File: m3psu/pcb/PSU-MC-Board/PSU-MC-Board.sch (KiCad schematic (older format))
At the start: 53 parts

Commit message: Remove JTAG programmer connection from MCU board
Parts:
- removed P?: SWD_TC, agg:TC2030-NL, symbol SWD_TC
- added R? (x2): R, symbol R
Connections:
- net labels removed: ~RST
- wire segments 307 -> 385

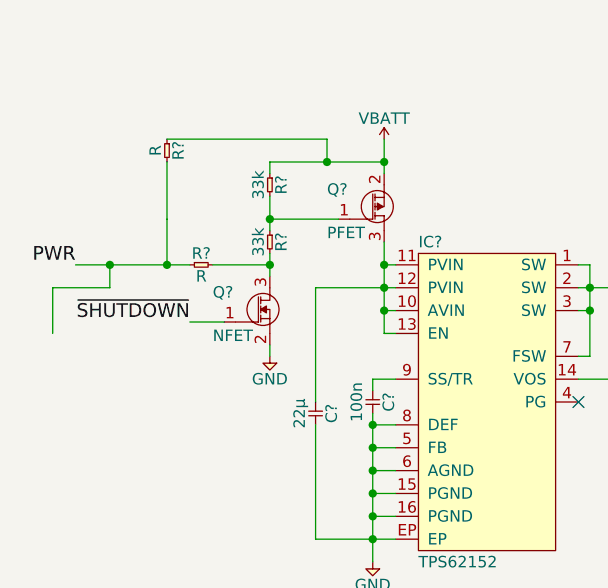
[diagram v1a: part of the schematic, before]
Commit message: Minor changes for uniformity for DC/DC converters.
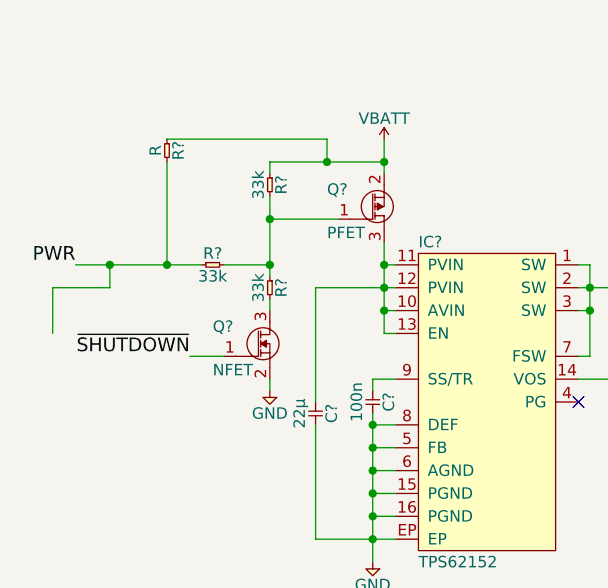
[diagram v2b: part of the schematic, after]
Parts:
- removed R?: 33k, agg:0402, symbol R
- removed R?: R, symbol R
- added R? (x2): 33k, agg:0402, symbol R
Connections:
- net PWR: now also R?.1
- net at Q?.1 (G), R?.2: now also R?.1, R?.2
- net at Q?.3 (D): now also R?.2
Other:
- moved on the sheet: Q?
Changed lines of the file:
@@
 EESchema Schematic File Version 2
 LIBS:agg-kicad
+LIBS:PSU-MC-Board-cache
 EELAYER 25 0
 EELAYER END
@@
 L NFET Q?
 U 1 1 56E1C0D3
-P 1600 1800
-F 0 "Q?" H 1350 1830 50  0000 L CNN
-F 1 "NFET" H 1350 1640 50  0000 L CNN
-F 2 "agg:SOT-883-B" H 1600 1800 50  0001 C CNN
-F 3 "http://www.nxp.com/documents/data_sheet/PMZB150UNE.pdf" H 1600 1800 50  0001 C CNN
-F 4 "2498598" H 1600 1800 60  0001 C CNN "Farnell"
-	1    1600 1800
+P 1600 1950
+F 0 "Q?" H 1350 1980 50  0000 L CNN
+F 1 "NFET" H 1350 1790 50  0000 L CNN
+F 2 "agg:SOT-883-B" H 1600 1950 50  0001 C CNN
+F 3 "http://www.nxp.com/documents/data_sheet/PMZB150UNE.pdf" H 1600 1950 50  0001 C CNN
+F 4 "2498598" H 1600 1950 60  0001 C CNN "Farnell"
+	1    1600 1950
 	1    0    0    -1
 $EndComp
@@
 $EndComp
 $Comp
-L R R?
-U 1 1 56E3210E
-P 1600 1500
-F 0 "R?" H 1650 1550 50  0000 C CNN
-F 1 "33k" H 1650 1450 50  0000 C CNN
-F 2 "agg:0402" H 1600 1500 50  0001 C CNN
-F 3 "" H 1600 1500 50  0001 C CNN
-F 4 "2447160" H 1600 1500 60  0001 C CNN "Farnell"
-	1    1600 1500
-	0    1    1    0
-$EndComp
-$Comp
 L GND #PWR020
 U 1 1 56E3524C
-P 1600 2050
-F 0 "#PWR020" H 1470 2090 50  0001 L CNN
-F 1 "GND" H 1600 1950 50  0000 C CNN
-F 2 "" H 1600 2050 60  0000 C CNN
-F 3 "" H 1600 2050 60  0000 C CNN
-	1    1600 2050
+P 1600 2200
+F 0 "#PWR020" H 1470 2240 50  0001 L CNN
+F 1 "GND" H 1600 2100 50  0000 C CNN
+F 2 "" H 1600 2200 60  0000 C CNN
+F 3 "" H 1600 2200 60  0000 C CNN
+	1    1600 2200
 	-1   0    0    -1
 $EndComp
 Text Label 750  1650 2    60   ~ 0
 PWR
-Text Label 1250 1900 2    60   ~ 0
+Text Label 1250 2050 2    60   ~ 0
 ~SHUTDOWN
 $Comp
@@
 	2100 1200 2100 1250
 Wire Wire Line
-	2100 1200 1850 1200
-Wire Wire Line
-	1850 1200 1600 1200
+	1600 1200 1850 1200
+Wire Wire Line
+	1850 1200 2100 1200
 Wire Wire Line
 	1600 1200 1600 1250
@@
 	1600 1350 1600 1450
 Wire Wire Line
-	1600 1450 1600 1500
-Wire Wire Line
-	1600 1600 1600 1650
+	1600 1450 1600 1650
 Wire Wire Line
 	1600 1650 1600 1700
@@
 Connection ~ 1600 1450
 Wire Wire Line
-	1600 2000 1600 2050
+	1600 2150 1600 2200
 Connection ~ 1600 1650
 Wire Wire Line
-	1400 1900 1250 1900
+	1400 2050 1250 2050
 Wire Wire Line
 	8800 700  8800 750
@@
 Connection ~ 9050 4250
 Wire Wire Line
-	1150 1200 1150 1450
-$Comp
-L R R?
-U 1 1 56E3DB52
-P 1250 1650
-F 0 "R?" H 1300 1700 50  0000 C CNN
-F 1 "R" H 1300 1600 50  0000 C CNN
-F 2 "" H 1250 1650 50  0001 C CNN
-F 3 "" H 1250 1650 50  0001 C CNN
-	1    1250 1650
-	1    0    0    -1
-$EndComp
-Wire Wire Line
-	1350 1650 1600 1650
-Wire Wire Line
-	1250 1650 1150 1650
-Wire Wire Line
-	1150 1650 900  1650
-Wire Wire Line
-	900  1650 750  1650
+	1150 1200 1150 1650
+Wire Wire Line
+	1400 1650 1600 1650
+Wire Wire Line
+	750  1650 900  1650
+Wire Wire Line
+	900  1650 1150 1650
+Wire Wire Line
+	1150 1650 1300 1650
 Wire Wire Line
 	900  1650 900  1750
@@
 	1850 1100 1850 1200
 Connection ~ 1850 1200
-Wire Wire Line
-	1150 1450 1150 1450
-Wire Wire Line
-	1150 1450 1150 1650
 Connection ~ 1150 1650
+Wire Wire Line
+	1600 1800 1600 1850
+$Comp
+L R R?
+U 1 1 56E2D4E9
+P 1600 1700
+F 0 "R?" H 1650 1750 50  0000 C CNN
+F 1 "33k" H 1650 1650 50  0000 C CNN
+F 2 "agg:0402" H 1600 1700 50  0001 C CNN
+F 3 "" H 1600 1700 50  0001 C CNN
+F 4 "2447160" H 1600 1700 60  0001 C CNN "Farnell"
+	1    1600 1700
+	0    1    1    0
+$EndComp
+$Comp
+L R R?
+U 1 1 56E2D5A8
+P 1300 1650
+F 0 "R?" H 1350 1700 50  0000 C CNN
+F 1 "33k" H 1350 1600 50  0000 C CNN
+F 2 "agg:0402" H 1300 1650 50  0001 C CNN
+F 3 "" H 1300 1650 50  0001 C CNN
+F 4 "2447160" H 1300 1650 60  0001 C CNN "Farnell"
+	1    1300 1650
+	1    0    0    -1
+$EndComp
 $EndSCHEMATC

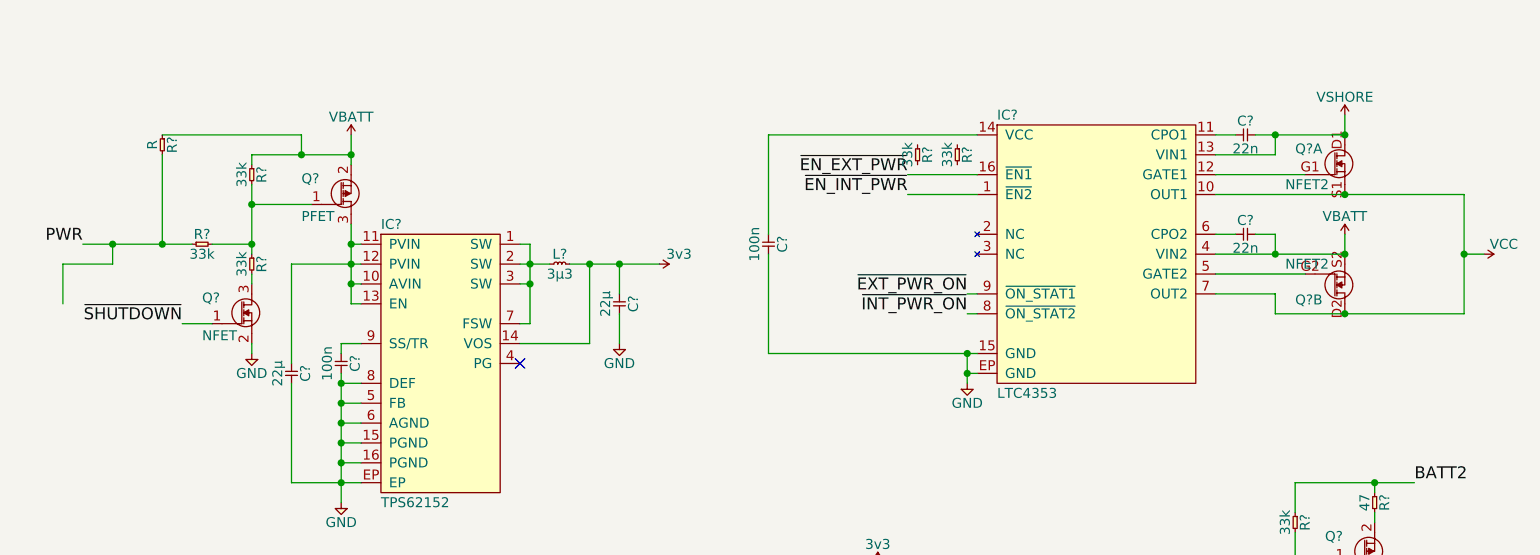
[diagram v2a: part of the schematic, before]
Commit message: Trying to resolve complete shutdown problem.
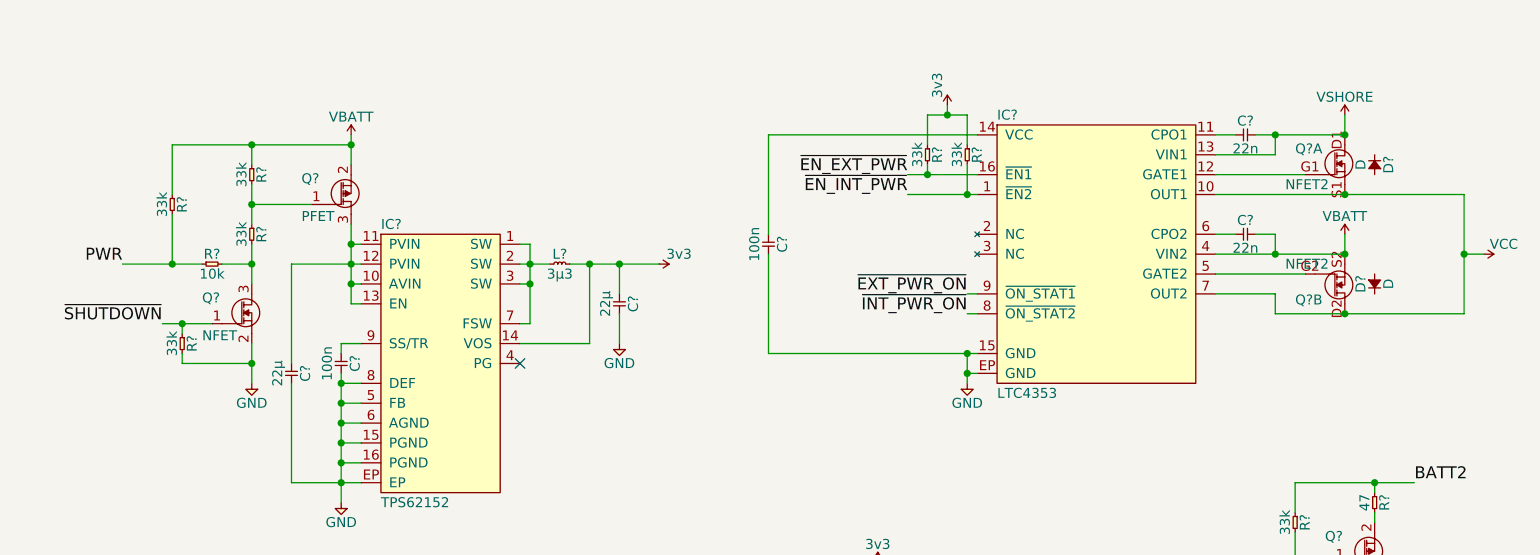
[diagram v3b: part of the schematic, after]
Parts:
- added D? (x2): D, symbol D
- added R?: 33k, agg:0402, symbol R
- R?: value 33k -> 10k; Farnell 2447160 -> 2447096
- R?: value R -> 33k; footprint (none) -> agg:0402
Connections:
- net 3v3: now also R?.1, R?.1
- net GND: now also R?.2
- net ~EN_EXT_PWR: now also R?.2
- net ~EN_INT_PWR: now also R?.2
- net ~SHUTDOWN: now also R?.1
- net at Q?.1 (G), R?.1, R?.2: no longer R?.2
- net at Q?.3 (D), R?.2: now also R?.2
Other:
- moved on the sheet: R?
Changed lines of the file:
@@
 L GND #PWR020
 U 1 1 56E3524C
-P 1600 2200
-F 0 "#PWR020" H 1470 2240 50  0001 L CNN
-F 1 "GND" H 1600 2100 50  0000 C CNN
-F 2 "" H 1600 2200 60  0000 C CNN
-F 3 "" H 1600 2200 60  0000 C CNN
-	1    1600 2200
+P 1600 2350
+F 0 "#PWR020" H 1470 2390 50  0001 L CNN
+F 1 "GND" H 1600 2250 50  0000 C CNN
+F 2 "" H 1600 2350 60  0000 C CNN
+F 3 "" H 1600 2350 60  0000 C CNN
+	1    1600 2350
 	-1   0    0    -1
 $EndComp
-Text Label 750  1650 2    60   ~ 0
+Text Label 950  1750 2    60   ~ 0
 PWR
-Text Label 1250 2050 2    60   ~ 0
+Text Label 1150 2050 2    60   ~ 0
 ~SHUTDOWN
 $Comp
@@
 L R R?
 U 1 1 56E53787
-P 5150 1150
-F 0 "R?" H 5200 1200 50  0000 C CNN
-F 1 "33k" H 5200 1100 50  0000 C CNN
-F 2 "agg:0402" H 5150 1150 50  0001 C CNN
-F 3 "" H 5150 1150 50  0001 C CNN
-F 4 "2447160" H 5150 1150 60  0001 C CNN "Farnell"
-	1    5150 1150
+P 5200 1150
+F 0 "R?" H 5250 1200 50  0000 C CNN
+F 1 "33k" H 5250 1100 50  0000 C CNN
+F 2 "agg:0402" H 5200 1150 50  0001 C CNN
+F 3 "" H 5200 1150 50  0001 C CNN
+F 4 "2447160" H 5200 1150 60  0001 C CNN "Farnell"
+	1    5200 1150
 	0    1    1    0
 $EndComp
@@
 L R R?
 U 1 1 56E53C49
-P 4950 1150
-F 0 "R?" H 5000 1200 50  0000 C CNN
-F 1 "33k" H 5000 1100 50  0000 C CNN
-F 2 "agg:0402" H 4950 1150 50  0001 C CNN
-F 3 "" H 4950 1150 50  0001 C CNN
-F 4 "2447160" H 4950 1150 60  0001 C CNN "Farnell"
-	1    4950 1150
+P 5000 1150
+F 0 "R?" H 5050 1200 50  0000 C CNN
+F 1 "33k" H 5050 1100 50  0000 C CNN
+F 2 "agg:0402" H 5000 1150 50  0001 C CNN
+F 3 "" H 5000 1150 50  0001 C CNN
+F 4 "2447160" H 5000 1150 60  0001 C CNN "Farnell"
+	1    5000 1150
 	0    1    1    0
 $EndComp
@@
 L R R?
 U 1 1 56E390EF
-P 1150 1100
-F 0 "R?" H 1200 1150 50  0000 C CNN
-F 1 "R" H 1200 1050 50  0000 C CNN
-F 2 "" H 1150 1100 50  0001 C CNN
-F 3 "" H 1150 1100 50  0001 C CNN
-	1    1150 1100
+P 1200 1400
+F 0 "R?" H 1250 1450 50  0000 C CNN
+F 1 "33k" H 1250 1350 50  0000 C CNN
+F 2 "agg:0402" H 1200 1400 50  0001 C CNN
+F 3 "2447160" H 1200 1400 50  0001 C CNN
+	1    1200 1400
 	0    1    1    0
 $EndComp
@@
 	5250 1900 5200 1900
 Wire Wire Line
-	5250 1400 4900 1400
-Wire Wire Line
-	5250 1300 4900 1300
+	5250 1400 5200 1400
+Wire Wire Line
+	5200 1400 4900 1400
+Wire Wire Line
+	5250 1300 5000 1300
+Wire Wire Line
+	5000 1300 4900 1300
 Wire Wire Line
 	6450 1700 6750 1700
@@
 Connection ~ 3450 1750
 Wire Wire Line
-	2100 1100 2100 1200
-Wire Wire Line
-	2100 1200 2100 1250
-Wire Wire Line
-	1600 1200 1850 1200
-Wire Wire Line
-	1850 1200 2100 1200
-Wire Wire Line
-	1600 1200 1600 1250
-Connection ~ 2100 1200
+	2100 1100 2100 1150
+Wire Wire Line
+	2100 1150 2100 1250
+Wire Wire Line
+	1200 1150 1600 1150
+Wire Wire Line
+	1600 1150 2100 1150
+Wire Wire Line
+	1600 1150 1600 1250
+Connection ~ 2100 1150
 Wire Wire Line
 	1600 1350 1600 1450
 Wire Wire Line
-	1600 1450 1600 1650
-Wire Wire Line
-	1600 1650 1600 1700
-Wire Wire Line
-	1900 1450 1600 1450
+	1600 1450 1600 1550
+Wire Wire Line
+	1600 1450 1900 1450
 Connection ~ 1600 1450
 Wire Wire Line
-	1600 2150 1600 2200
-Connection ~ 1600 1650
-Wire Wire Line
-	1400 2050 1250 2050
+	1600 2150 1600 2250
+Wire Wire Line
+	1600 2250 1600 2350
+Wire Wire Line
+	1150 2050 1250 2050
+Wire Wire Line
+	1250 2050 1400 2050
 Wire Wire Line
 	8800 700  8800 750
@@
 Connection ~ 9050 4250
 Wire Wire Line
-	1150 1200 1150 1650
-Wire Wire Line
-	1400 1650 1600 1650
-Wire Wire Line
-	750  1650 900  1650
-Wire Wire Line
-	900  1650 1150 1650
-Wire Wire Line
-	1150 1650 1300 1650
-Wire Wire Line
-	900  1650 900  1750
-Wire Wire Line
-	900  1750 650  1750
-Wire Wire Line
-	650  1750 650  1950
-Connection ~ 900  1650
-Wire Wire Line
-	1150 1100 1850 1100
-Wire Wire Line
-	1850 1100 1850 1200
-Connection ~ 1850 1200
-Connection ~ 1150 1650
-Wire Wire Line
-	1600 1800 1600 1850
+	1200 1750 1200 1500
+Wire Wire Line
+	1600 1650 1600 1750
+Wire Wire Line
+	1600 1750 1600 1850
 $Comp
 L R R?
 U 1 1 56E2D4E9
-P 1600 1700
-F 0 "R?" H 1650 1750 50  0000 C CNN
-F 1 "33k" H 1650 1650 50  0000 C CNN
-F 2 "agg:0402" H 1600 1700 50  0001 C CNN
-F 3 "" H 1600 1700 50  0001 C CNN
-F 4 "2447160" H 1600 1700 60  0001 C CNN "Farnell"
-	1    1600 1700
+P 1600 1550
+F 0 "R?" H 1650 1600 50  0000 C CNN
+F 1 "33k" H 1650 1500 50  0000 C CNN
+F 2 "agg:0402" H 1600 1550 50  0001 C CNN
+F 3 "" H 1600 1550 50  0001 C CNN
+F 4 "2447160" H 1600 1550 60  0001 C CNN "Farnell"
+	1    1600 1550
 	0    1    1    0
 $EndComp
@@
 L R R?
 U 1 1 56E2D5A8
-P 1300 1650
-F 0 "R?" H 1350 1700 50  0000 C CNN
-F 1 "33k" H 1350 1600 50  0000 C CNN
-F 2 "agg:0402" H 1300 1650 50  0001 C CNN
-F 3 "" H 1300 1650 50  0001 C CNN
-F 4 "2447160" H 1300 1650 60  0001 C CNN "Farnell"
-	1    1300 1650
-	1    0    0    -1
+P 1350 1750
+F 0 "R?" H 1400 1800 50  0000 C CNN
+F 1 "10k" H 1400 1700 50  0000 C CNN
+F 2 "agg:0402" H 1350 1750 50  0001 C CNN
+F 3 "" H 1350 1750 50  0001 C CNN
+F 4 "2447096" H 1350 1750 60  0001 C CNN "Farnell"
+	1    1350 1750
+	1    0    0    -1
+$EndComp
+Wire Wire Line
+	1200 1400 1200 1150
+Connection ~ 1600 1150
+Wire Wire Line
+	1450 1750 1600 1750
+Connection ~ 1600 1750
+Wire Wire Line
+	950  1750 1200 1750
+Wire Wire Line
+	1200 1750 1350 1750
+Connection ~ 1200 1750
+$Comp
+L R R?
+U 1 1 56E4F490
+P 1250 2100
+F 0 "R?" H 1300 2150 50  0000 C CNN
+F 1 "33k" H 1300 2050 50  0000 C CNN
+F 2 "agg:0402" H 1250 2100 50  0001 C CNN
+F 3 "2447160" H 1250 2100 50  0001 C CNN
+	1    1250 2100
+	0    1    1    0
+$EndComp
+Wire Wire Line
+	1250 2100 1250 2050
+Connection ~ 1250 2050
+Wire Wire Line
+	1250 2200 1250 2250
+Wire Wire Line
+	1250 2250 1600 2250
+Connection ~ 1600 2250
+Wire Wire Line
+	5000 1250 5000 1300
+Connection ~ 5000 1300
+Wire Wire Line
+	5200 1250 5200 1400
+Connection ~ 5200 1400
+$Comp
+L 3v3 #PWR?
+U 1 1 56E5731B
+P 5100 950
+F 0 "#PWR?" H 5100 1060 50  0001 L CNN
+F 1 "3v3" V 5050 1050 50  0000 C CNN
+F 2 "" H 5100 950 60  0000 C CNN
+F 3 "" H 5100 950 60  0000 C CNN
+	1    5100 950
+	1    0    0    -1
+$EndComp
+Wire Wire Line
+	5000 1150 5000 1000
+Wire Wire Line
+	5000 1000 5100 1000
+Wire Wire Line
+	5100 1000 5200 1000
+Wire Wire Line
+	5200 1000 5200 1150
+Wire Wire Line
+	5100 1000 5100 950
+Connection ~ 5100 1000
+$Comp
+L D D?
+U 1 1 56E2B7F5
+P 7250 1200
+F 0 "D?" H 7300 1270 50  0000 C CNN
+F 1 "D" H 7300 1130 50  0000 C CNN
+F 2 "" H 7250 1200 50  0001 C CNN
+F 3 "" H 7250 1200 50  0001 C CNN
+	1    7250 1200
+	0    1    1    0
+$EndComp
+$Comp
+L D D?
+U 1 1 56E2BA91
+P 7250 1900
+F 0 "D?" H 7300 1970 50  0000 C CNN
+F 1 "D" H 7300 1830 50  0000 C CNN
+F 2 "" H 7250 1900 50  0001 C CNN
+F 3 "" H 7250 1900 50  0001 C CNN
+	1    7250 1900
+	0    -1   -1   0
 $EndComp
 $EndSCHEMATC

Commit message: Tried routing the Microcontroller board.
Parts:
- removed D? (x2): D, symbol D
- added Q5: NFET2, agg:PowerFLAT5x6, symbol NFET2
- added R10: 4k7, agg:0402, symbol R
- C17, C18: renamed from C?; value 22n -> 47n; Farnell 2210825 -> 1828868
- gave numbers to parts that had none: 52
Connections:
- net 3v3: now also R10.1
- net SCL: now also IC1.41 (PA8)
- net SDA: now also IC1.40 (PC9)
- net VBATT: now also Q5.S1 (S); no longer Q4.S2 (S)
- net VCC: now also Q4.S2 (S), Q5.S2 (S); no longer Q4.D2 (D), Q4.S1 (S)
- net VSHORE: now also Q4.S1 (S); no longer Q4.D1 (D)
- net ~ALERT: now also IC1.42 (PA9), R10.2
- net at IC4.12 (GATE1): now also Q4.G1 (G), Q4.G2 (G); no longer Q4.G1 (G)
- net at IC4.5 (GATE2): now also Q5.G1 (G), Q5.G2 (G); no longer Q4.G2 (G)
- new net: Q4.D1 (D), Q4.D2 (D)
- new net: Q5.D1 (D), Q5.D2 (D)

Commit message: Finished routing PSU uC board. Just needs checking.
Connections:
- net BLEED_BATT1: now also IC1.25 (PC5)
- net BLEED_BATT2: now also IC1.24 (PC4)
- net EN_PYRO: now also IC1.16 (PA2)
- net ~EN_EXT_PWR: now also IC1.43 (PA10)
- net ~EN_INT_PWR: now also IC1.39 (PC8)
- net ~EXT_PWR_ON: now also IC1.44 (PA11)
- net ~INT_PWR_ON: now also IC1.45 (PA12)

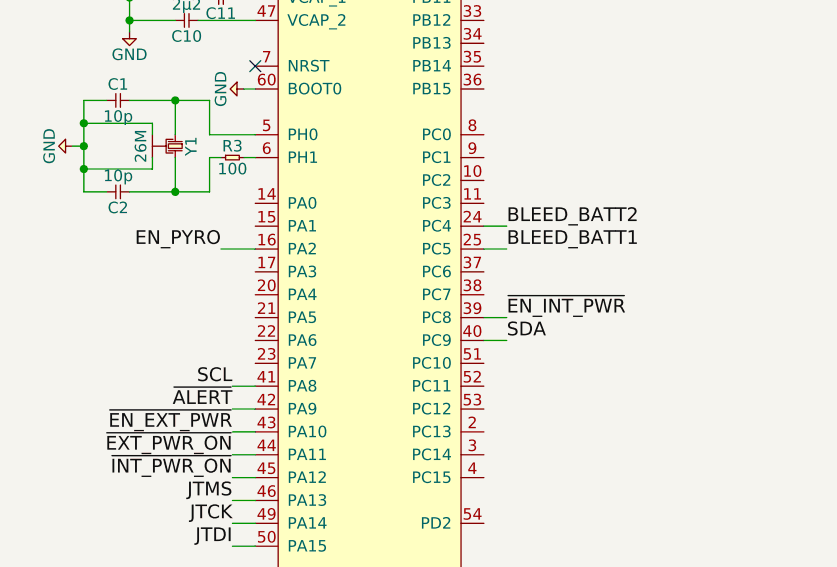
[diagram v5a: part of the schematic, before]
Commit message: Finished routing the Li-ion Charger board. Needs checking. Did a brief check of the MCU board. Not done yet.
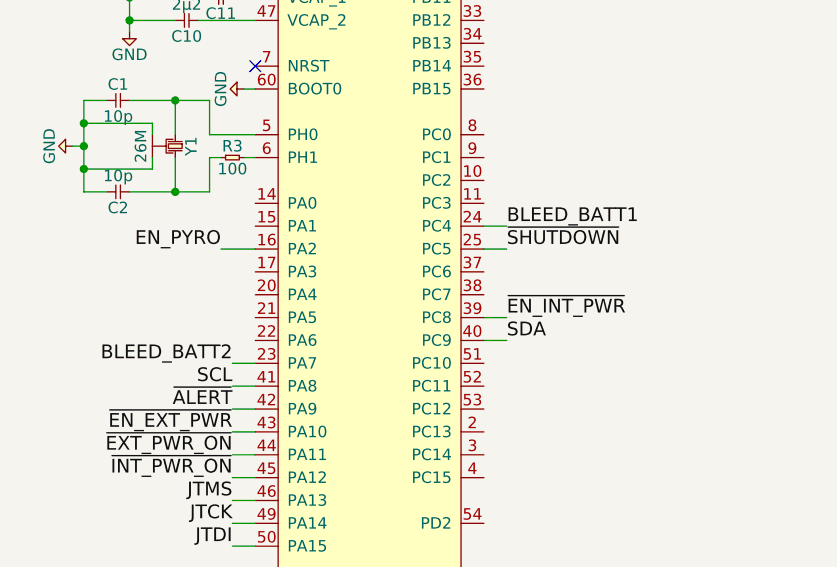
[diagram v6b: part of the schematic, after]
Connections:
- net BLEED_BATT1: now also IC1.24 (PC4); no longer IC1.25 (PC5)
- net BLEED_BATT2: now also IC1.23 (PA7); no longer IC1.24 (PC4)
- net ~SHUTDOWN: now also IC1.25 (PC5)
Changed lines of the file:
@@
 EESchema Schematic File Version 2
 LIBS:agg-kicad
+LIBS:PSU-MC-Board-cache
 EELAYER 25 0
 EELAYER END
@@
 Wire Wire Line
 	1300 6200 1450 6200
+Text Label 2550 6100 0    60   ~ 0
+BLEED_BATT1
+Text Label 1350 6700 2    60   ~ 0
+BLEED_BATT2
+Wire Wire Line
+	2550 6100 2450 6100
+Wire Wire Line
+	2450 6200 2550 6200
 Text Label 2550 6200 0    60   ~ 0
-BLEED_BATT1
-Text Label 2550 6100 0    60   ~ 0
-BLEED_BATT2
-Wire Wire Line
-	2550 6100 2450 6100
-Wire Wire Line
-	2450 6200 2550 6200
+~SHUTDOWN
+Wire Wire Line
+	1350 6700 1450 6700
 $EndSCHEMATC

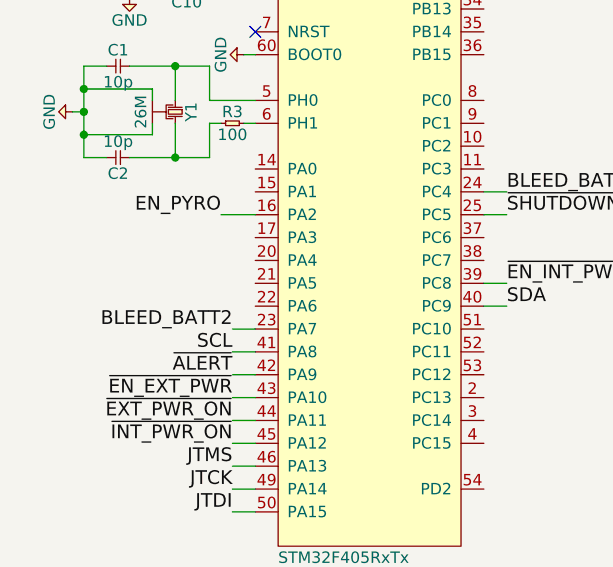
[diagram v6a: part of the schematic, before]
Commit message: Added on the battery voltage monitoring.
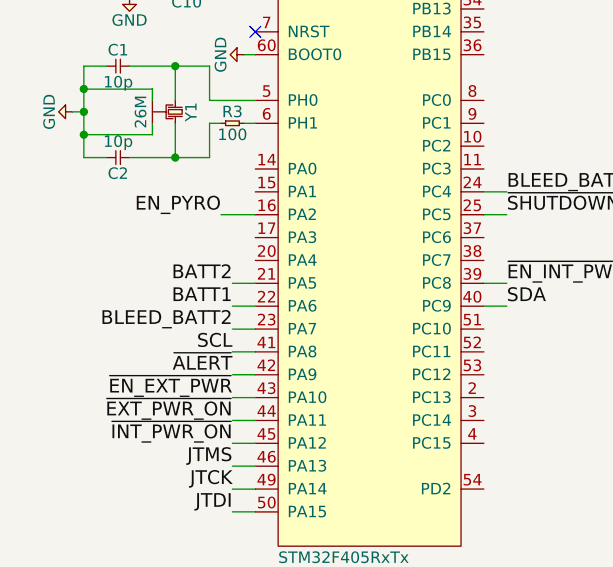
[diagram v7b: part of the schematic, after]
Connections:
- net BATT1: now also IC1.22 (PA6)
- net BATT2: now also IC1.21 (PA5)
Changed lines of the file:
@@
 Wire Wire Line
 	1350 6700 1450 6700
+Text Label 1350 6600 2    60   ~ 0
+BATT1
+Wire Wire Line
+	1350 6600 1450 6600
+Text Label 1350 6500 2    60   ~ 0
+BATT2
+Wire Wire Line
+	1350 6500 1450 6500
 $EndSCHEMATC
